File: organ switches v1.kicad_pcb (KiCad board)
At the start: 2 copper layers, 20 parts, among them SW1 SW_SPST, SW10 SW_SPST, SW11 SW_SPST, SW12 SW_SPST, SW13 SW_SPST, SW14 SW_SPST, SW15 SW_SPST, SW16 SW_SPST, SW2 SW_SPST, SW3 SW_SPST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

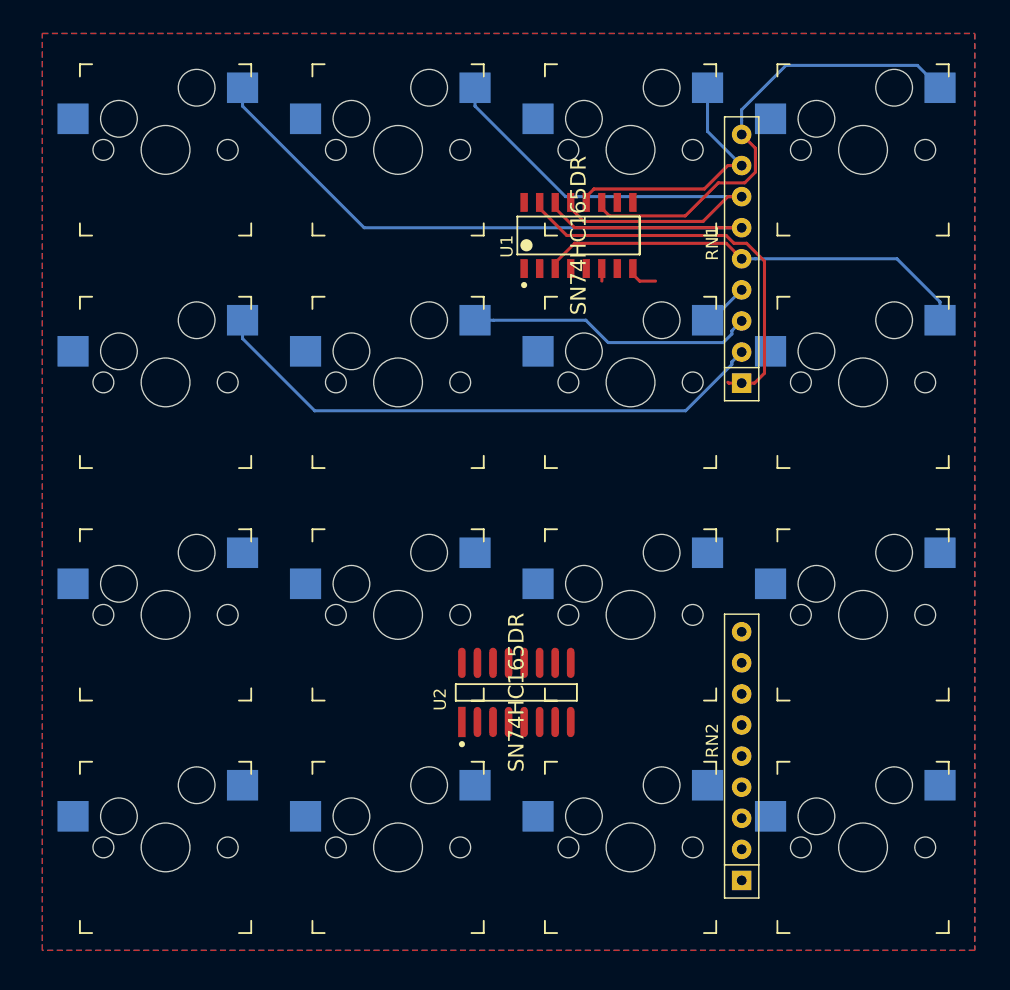
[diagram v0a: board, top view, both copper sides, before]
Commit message: pcb component layout complete, no traces
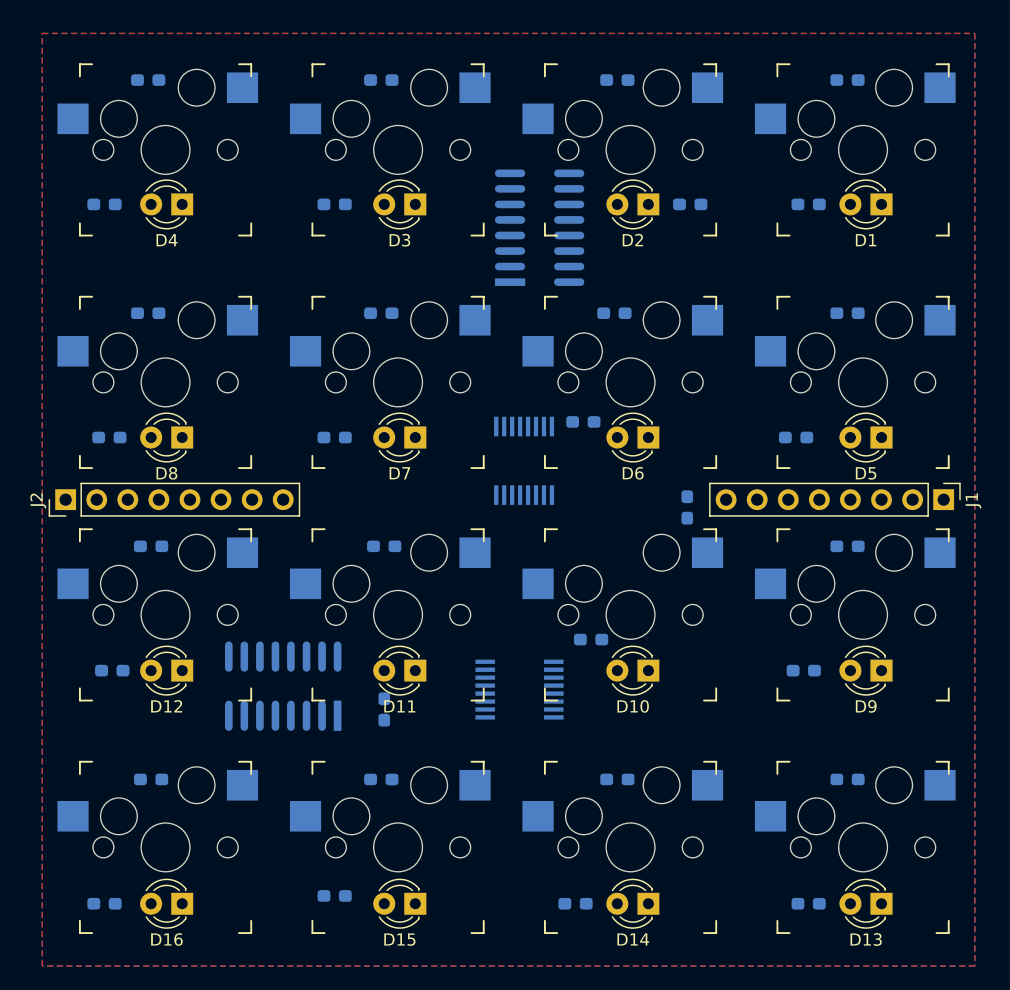
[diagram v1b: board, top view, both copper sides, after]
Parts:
- removed RN1, RN2: R_Network08_US, Resistor_THT:R_Array_SIP9
- added D1: LED, LED_THT:LED_D3.0mm, F.Cu at (270.5, 84.5)
- added D10: LED, LED_THT:LED_D3.0mm, F.Cu at (251.5, 122.6)
- added D11: LED, LED_THT:LED_D3.0mm, F.Cu at (232.4, 122.6)
- added D12: LED, LED_THT:LED_D3.0mm, F.Cu at (213.4, 122.6)
- added D13: LED, LED_THT:LED_D3.0mm, F.Cu at (270.5, 141.6)
- added D14: LED, LED_THT:LED_D3.0mm, F.Cu at (251.5, 141.6)
- added D15: LED, LED_THT:LED_D3.0mm, F.Cu at (232.4, 141.6)
- added D16: LED, LED_THT:LED_D3.0mm, F.Cu at (213.4, 141.6)
- added D2: LED, LED_THT:LED_D3.0mm, F.Cu at (251.5, 84.5)
- added D3: LED, LED_THT:LED_D3.0mm, F.Cu at (232.4, 84.5)
- added D4: LED, LED_THT:LED_D3.0mm, F.Cu at (213.4, 84.5)
- added D5: LED, LED_THT:LED_D3.0mm, F.Cu at (270.5, 103.5)
- added D6: LED, LED_THT:LED_D3.0mm, F.Cu at (251.5, 103.5)
- added D7: LED, LED_THT:LED_D3.0mm, F.Cu at (232.4, 103.5)
- added D8: LED, LED_THT:LED_D3.0mm, F.Cu at (213.4, 103.5)
- added D9: LED, LED_THT:LED_D3.0mm, F.Cu at (270.5, 122.6)
- added J1: Conn_01x08, Connector_PinHeader_2.54mm:PinHeader_1x08_P2.54mm_Vertical, F.Cu at (275.6, 108.6)
- added J2: Conn_01x08, Connector_PinHeader_2.54mm:PinHeader_1x08_P2.54mm_Vertical, F.Cu at (203.8, 108.6)
- added R1: 150, Resistor_SMD:R_0603_1608Metric_Pad1.05x0.95mm_HandSolder, B.Cu at (264.6, 84.5)
- added R10: 150, Resistor_SMD:R_0603_1608Metric_Pad1.05x0.95mm_HandSolder, B.Cu at (246.8, 120.0)
- added R11: 150, Resistor_SMD:R_0603_1608Metric_Pad1.05x0.95mm_HandSolder, B.Cu at (229.9, 125.7)
- added R12: 150, Resistor_SMD:R_0603_1608Metric_Pad1.05x0.95mm_HandSolder, B.Cu at (207.6, 122.6)
- added R13: 150, Resistor_SMD:R_0603_1608Metric_Pad1.05x0.95mm_HandSolder, B.Cu at (264.6, 141.6)
- added R14: 150, Resistor_SMD:R_0603_1608Metric_Pad1.05x0.95mm_HandSolder, B.Cu at (245.5, 141.6)
- added R15: 150, Resistor_SMD:R_0603_1608Metric_Pad1.05x0.95mm_HandSolder, B.Cu at (225.8, 141.0)
- added R16: 150, Resistor_SMD:R_0603_1608Metric_Pad1.05x0.95mm_HandSolder, B.Cu at (207.0, 141.6)
- added R17: 10K, Resistor_SMD:R_0603_1608Metric_Pad1.05x0.95mm_HandSolder, B.Cu at (267.7, 74.3)
- added R18: 10K, Resistor_SMD:R_0603_1608Metric_Pad1.05x0.95mm_HandSolder, B.Cu at (248.9, 74.3)
- added R19: 10K, Resistor_SMD:R_0603_1608Metric_Pad1.05x0.95mm_HandSolder, B.Cu at (229.6, 74.3)
- added R2: 150, Resistor_SMD:R_0603_1608Metric_Pad1.05x0.95mm_HandSolder, B.Cu at (254.9, 84.5)
- added R20: 10K, Resistor_SMD:R_0603_1608Metric_Pad1.05x0.95mm_HandSolder, B.Cu at (210.6, 74.3)
- added R21: 10K, Resistor_SMD:R_0603_1608Metric_Pad1.05x0.95mm_HandSolder, B.Cu at (267.7, 93.3)
- added R22: 10K, Resistor_SMD:R_0603_1608Metric_Pad1.05x0.95mm_HandSolder, B.Cu at (248.7, 93.3)
- added R23: 10K, Resistor_SMD:R_0603_1608Metric_Pad1.05x0.95mm_HandSolder, B.Cu at (229.6, 93.3)
- added R24: 10K, Resistor_SMD:R_0603_1608Metric_Pad1.05x0.95mm_HandSolder, B.Cu at (210.6, 93.3)
- added R25: 10K, Resistor_SMD:R_0603_1608Metric_Pad1.05x0.95mm_HandSolder, B.Cu at (267.7, 112.4)
- added R26: 10K, Resistor_SMD:R_0603_1608Metric_Pad1.05x0.95mm_HandSolder, B.Cu at (254.6, 109.2)
- added R27: 10K, Resistor_SMD:R_0603_1608Metric_Pad1.05x0.95mm_HandSolder, B.Cu at (229.9, 112.4)
- added R28: 10K, Resistor_SMD:R_0603_1608Metric_Pad1.05x0.95mm_HandSolder, B.Cu at (210.8, 112.4)
- added R29: 10K, Resistor_SMD:R_0603_1608Metric_Pad1.05x0.95mm_HandSolder, B.Cu at (267.7, 131.4)
- added R3: 150, Resistor_SMD:R_0603_1608Metric_Pad1.05x0.95mm_HandSolder, B.Cu at (225.8, 84.5)
- added R30: 10K, Resistor_SMD:R_0603_1608Metric_Pad1.05x0.95mm_HandSolder, B.Cu at (248.9, 131.4)
- added R31: 10K, Resistor_SMD:R_0603_1608Metric_Pad1.05x0.95mm_HandSolder, B.Cu at (229.6, 131.4)
- added R32: 10K, Resistor_SMD:R_0603_1608Metric_Pad1.05x0.95mm_HandSolder, B.Cu at (210.8, 131.4)
- added R4: 150, Resistor_SMD:R_0603_1608Metric_Pad1.05x0.95mm_HandSolder, B.Cu at (207.0, 84.5)
- added R5: 150, Resistor_SMD:R_0603_1608Metric_Pad1.05x0.95mm_HandSolder, B.Cu at (263.5, 103.5)
- added R6: 150, Resistor_SMD:R_0603_1608Metric_Pad1.05x0.95mm_HandSolder, B.Cu at (246.1, 102.2)
- added R7: 150, Resistor_SMD:R_0603_1608Metric_Pad1.05x0.95mm_HandSolder, B.Cu at (225.8, 103.5)
- added R8: 150, Resistor_SMD:R_0603_1608Metric_Pad1.05x0.95mm_HandSolder, B.Cu at (207.4, 103.5)
- added R9: 150, Resistor_SMD:R_0603_1608Metric_Pad1.05x0.95mm_HandSolder, B.Cu at (264.2, 122.6)
- added U3: TLC6C598QPWRQ1, eec:Texas_Instruments-PW0016A-0-0-0, B.Cu at (241.3, 105.4)
- added U4: TLC6C598QPWRQ1, eec:Texas_Instruments-PW0016A-0-0-0, B.Cu at (240.9, 124.1)
- U1: value SN74HC165DR -> 74HC165; footprint eec:Texas_Instruments-D0016A-0-0-MFG -> eec:Texas_Instruments-D0016A-0-0-IPC_A; moved to B.Cu
- U2: value SN74HC165DR -> 74HC165; moved to B.Cu
- moved U2 19.1 mm to (221.6, 123.8)
- moved U1 3.24 mm to (242.6, 86.4), turned to 0 degrees
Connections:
- U1 pad 1: Net-(U1-Pad1) -> Net-(J1-Pad3)
- U1 pad 16: Net-(U1-Pad16) -> +5V
- U1 pad 2: Net-(U1-Pad2) -> Net-(J1-Pad2)
- U2 pad 1: Net-(U2-Pad1) -> Net-(J1-Pad3)
- U2 pad 2: Net-(U2-Pad2) -> Net-(J1-Pad2)
- U2 pad 9: Net-(U2-Pad9) -> Net-(U1-Pad10)
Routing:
- net Net-(R20-Pad2): track 62.8 -> 0.00 mm
- net Net-(R24-Pad2): track 47.9 -> 0.00 mm
- net Net-(R19-Pad2): track 42.1 -> 0.00 mm
- net Net-(R17-Pad2): track 38.8 -> 0.03 mm
- net Net-(R21-Pad2): track 36.1 -> 0.00 mm
- net GND: track 35.7 -> 0.00 mm
- net Net-(R23-Pad2): track 23.9 -> 0.00 mm
- net Net-(R18-Pad2): track 21.7 -> 0.00 mm
- net Net-(R22-Pad2): track 4.29 -> 0.31 mm

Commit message: draft of traces
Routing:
- net Net-(J1-Pad3): track 0.00 -> 184.5 mm, vias 0 -> 3
- net Net-(J1-Pad2): track 0.00 -> 171.8 mm, vias 0 -> 6
- net GND: track 0.00 -> 100.1 mm, vias 0 -> 23
- net Net-(R25-Pad2): track 0.00 -> 87.7 mm, vias 0 -> 2
- net Net-(J1-Pad6): track 0.00 -> 75.7 mm, vias 0 -> 2
- net Net-(R20-Pad2): track 0.00 -> 72.9 mm, vias 0 -> 2
- net Net-(D4-Pad1): track 0.00 -> 68.7 mm, vias 0 -> 2
- net Net-(J1-Pad7): track 0.00 -> 65.0 mm, vias 0 -> 1
- net +5V: track 0.00 -> 60.2 mm, vias 0 -> 10
- net Net-(R29-Pad2): track 0.00 -> 59.9 mm
- net Net-(R26-Pad2): track 0.00 -> 58.6 mm, vias 0 -> 4
- net Net-(U1-Pad10): track 0.00 -> 57.7 mm, vias 0 -> 5
- net Net-(D13-Pad1): track 0.00 -> 53.0 mm, vias 0 -> 2
- net Net-(D16-Pad1): track 0.00 -> 48.0 mm, vias 0 -> 2
- net Net-(R21-Pad2): track 0.00 -> 47.6 mm, vias 0 -> 4
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
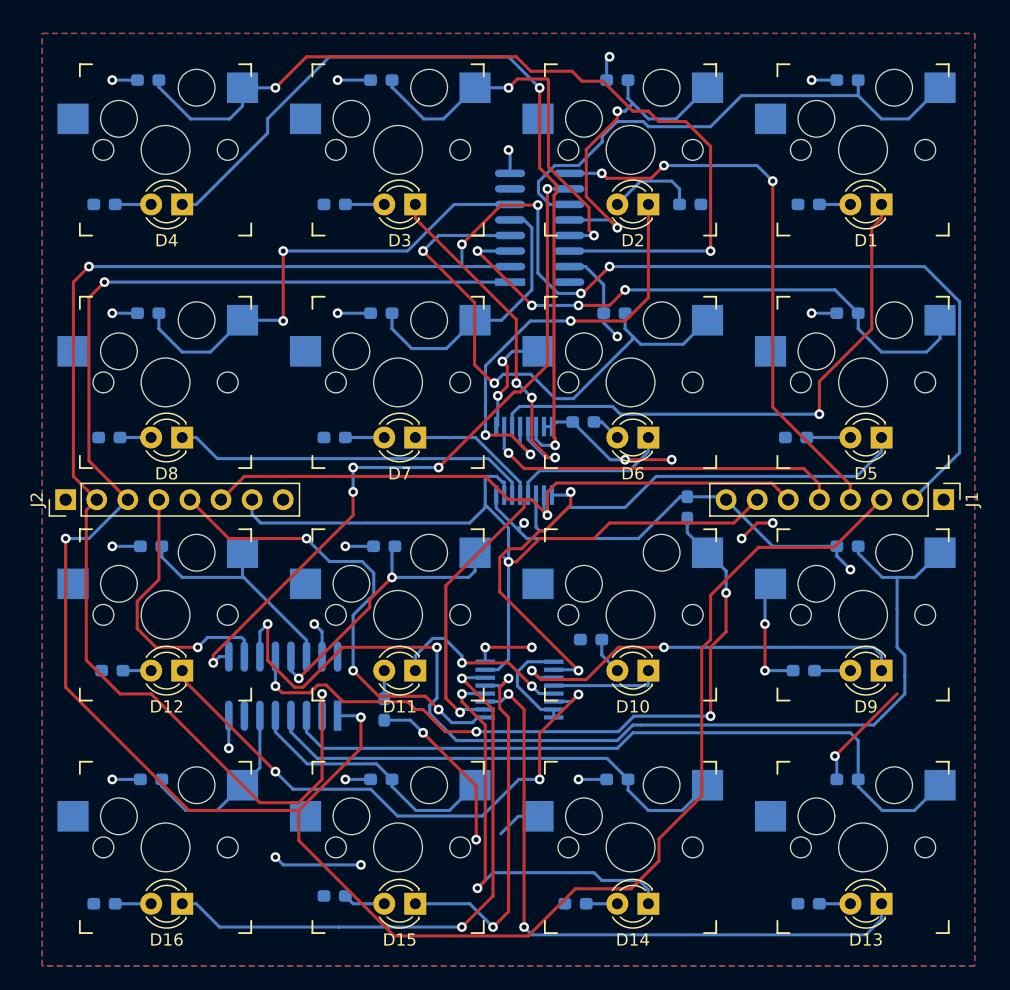
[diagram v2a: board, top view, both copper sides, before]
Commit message: addressed items 2, 5, 7, 9 from pinderh
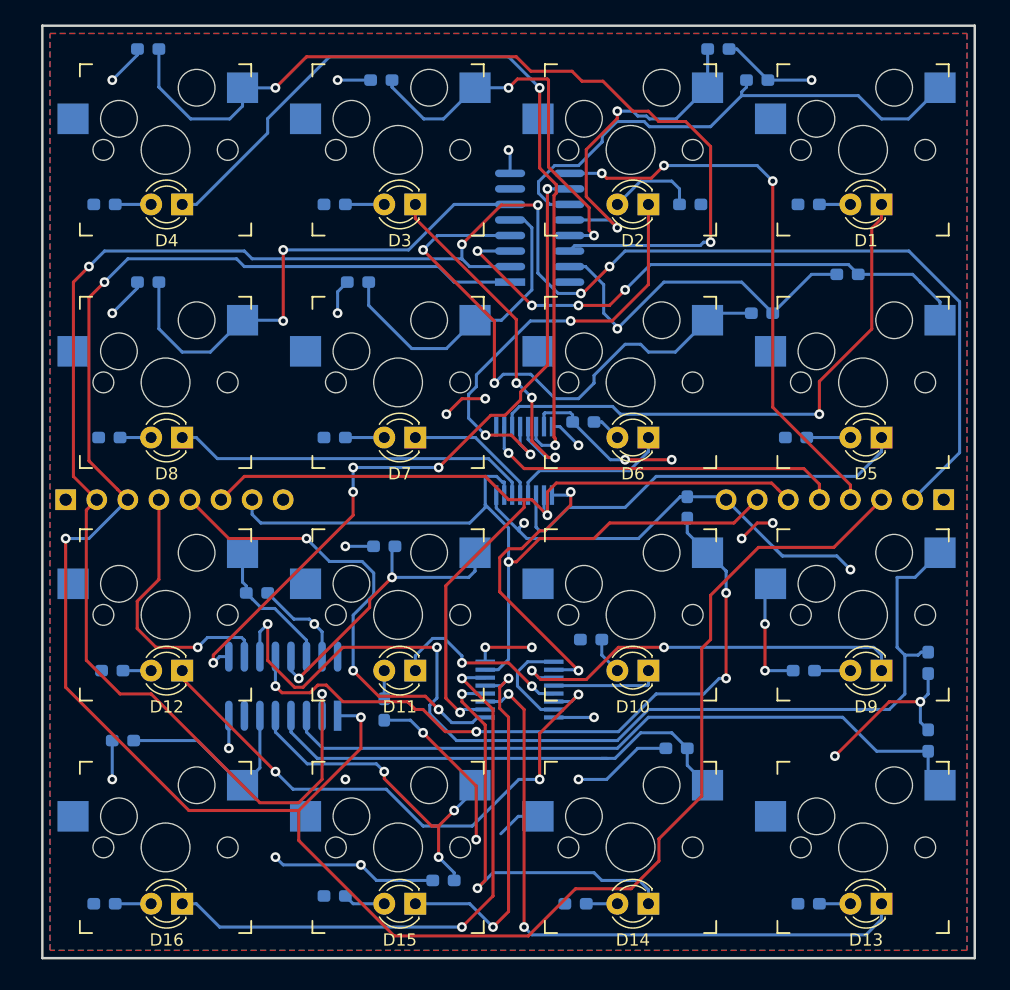
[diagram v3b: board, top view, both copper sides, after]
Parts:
- J1, J2: moved to B.Cu
- moved R22 12.1 mm to (260.7, 93.3), turned to 180 degrees
- moved R25 11.6 mm to (274.3, 121.9), turned to 90 degrees
- moved R31 9.69 mm to (234.7, 139.7)
- moved R28 9.45 mm to (219.5, 116.2), turned to 180 degrees
- moved R18 8.64 mm to (257.2, 71.8), turned to 180 degrees
- moved R17 7.38 mm to (260.4, 74.3), turned to 180 degrees
- moved R29 7.31 mm to (274.3, 128.3), turned to 270 degrees
- moved R30 5.47 mm to (253.8, 128.9)
- moved R32 3.92 mm to (208.5, 128.3)
- moved R21 3.17 mm to (267.7, 90.2)
- moved R23 3.17 mm to (227.7, 90.8)
- moved R20 2.54 mm to (210.6, 71.8)
- moved R24 2.54 mm to (210.6, 90.8)
- turned J1 to 90 degrees
- turned J2 to 270 degrees
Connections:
- U3 pad 8: +5V -> GND
- U4 pad 8: +5V -> GND
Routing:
- net GND: track 100.1 -> 151.3 mm
- net Net-(R28-Pad2): track 18.9 -> 11.3 mm
- net Net-(R31-Pad2): track 21.5 -> 27.7 mm, vias 0 -> 3
- net +5V: track 60.2 -> 55.8 mm
- net Net-(R23-Pad2): track 22.5 -> 25.8 mm
- net Net-(R24-Pad2): track 39.2 -> 41.7 mm
- net Net-(R25-Pad2): track 87.7 -> 85.1 mm
- net Net-(R20-Pad2): track 72.9 -> 75.0 mm
- net Net-(R22-Pad2): track 45.2 -> 47.1 mm
- net Net-(R29-Pad2): track 59.9 -> 58.1 mm
- net Net-(J1-Pad3): track 184.5 -> 186.1 mm
- net Net-(R32-Pad2): track 15.1 -> 16.7 mm
- net Net-(J1-Pad2): track 171.8 -> 173.3 mm
- net Net-(R21-Pad2): track 47.6 -> 46.5 mm
- net Net-(R26-Pad2): track 58.6 -> 57.6 mm
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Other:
- board outline added: 76.2 x 76.2 mm

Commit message: addressed item 8 from pinderh
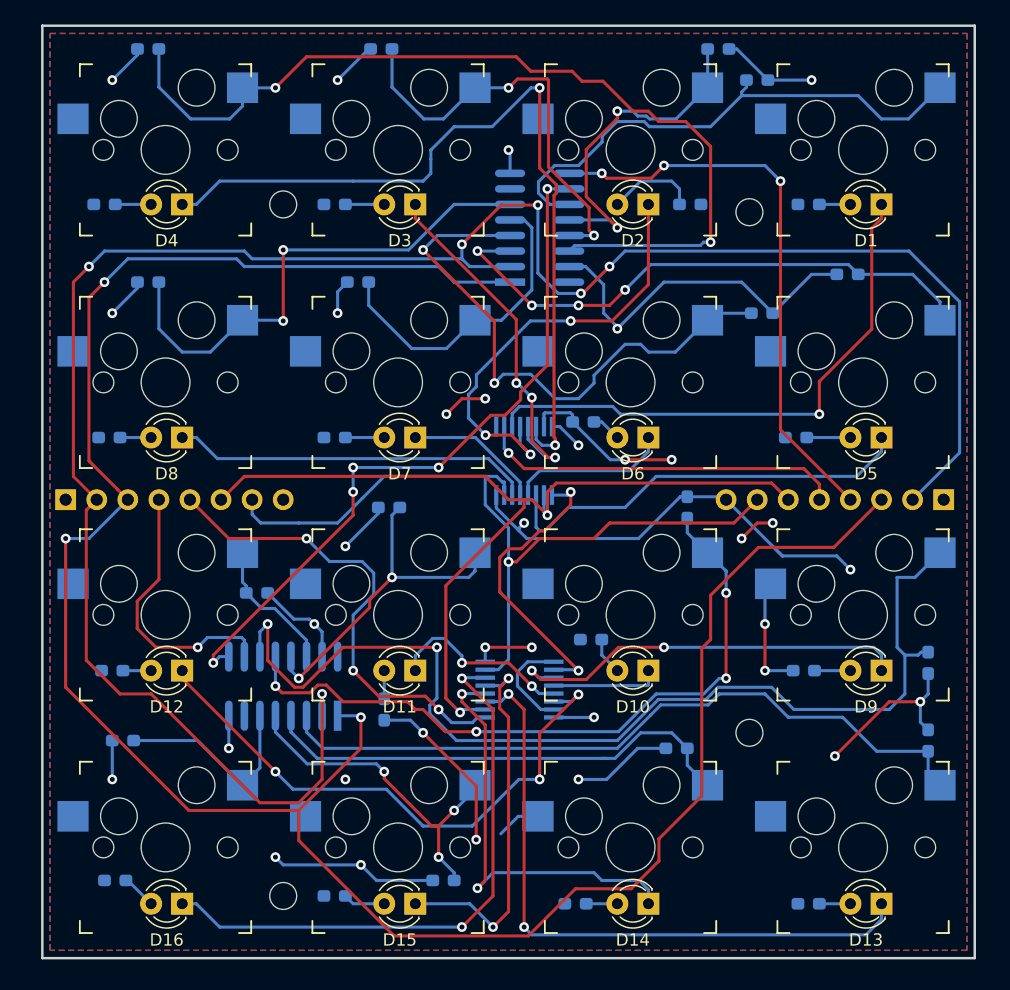
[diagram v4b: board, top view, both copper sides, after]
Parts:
- added ?: MountingHole_2.2mm_M2, MountingHole:MountingHole_2.2mm_M2, F.Cu at (221.6, 84.5)
- added ?: MountingHole_2.2mm_M2, MountingHole:MountingHole_2.2mm_M2, F.Cu at (259.7, 85.1)
- added ?: MountingHole_2.2mm_M2, MountingHole:MountingHole_2.2mm_M2, F.Cu at (259.7, 127.6)
- added ?: MountingHole_2.2mm_M2, MountingHole:MountingHole_2.2mm_M2, F.Cu at (221.6, 141.0)
- moved R27 3.20 mm to (230.3, 109.2)
- moved R19 2.54 mm to (229.6, 71.8)
- moved R16 2.10 mm to (207.9, 139.7)
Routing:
- net Net-(R27-Pad2): track 24.6 -> 27.9 mm
- net GND: track 151.3 -> 154.4 mm
- net Net-(R19-Pad2): track 32.1 -> 34.6 mm
- net Net-(D4-Pad1): track 68.7 -> 67.0 mm
- net Net-(R29-Pad2): track 58.1 -> 59.7 mm
- net Net-(R25-Pad2): track 85.1 -> 86.6 mm
- net Net-(J1-Pad7): track 64.5 -> 65.3 mm
